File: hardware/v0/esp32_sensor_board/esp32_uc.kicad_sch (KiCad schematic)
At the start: 25 parts, among them J301 USB_B_Micro, J302 Micro_SD_Card_Det, SW301 SW_SPST, U301 ESP32-C3, Y301 40 MHz, Y302 32kHz RTC Crystal

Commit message: Clean up errors
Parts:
- Y301: symbol Device:Crystal_GND24 -> BVH_Crystals:Crystal_GND24
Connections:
- net I2C_SCK: now also U301.10 (MTDI/GPIO5/ADC2_CH0)
- net I2C_SDA: now also U301.9 (MTMS/GPIO4/ADC1_CH4)
- net SD_CS: now also U301.21 (SPICS0/GPIO14)
- net SD_SCK: now also U301.22 (SPICLK/GPIO15)
- no-connect marks 0 -> 2
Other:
- moved on the sheet: C301, C302, C303, C304, C305, C306, C307, C308, C309, C310, C311, C312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

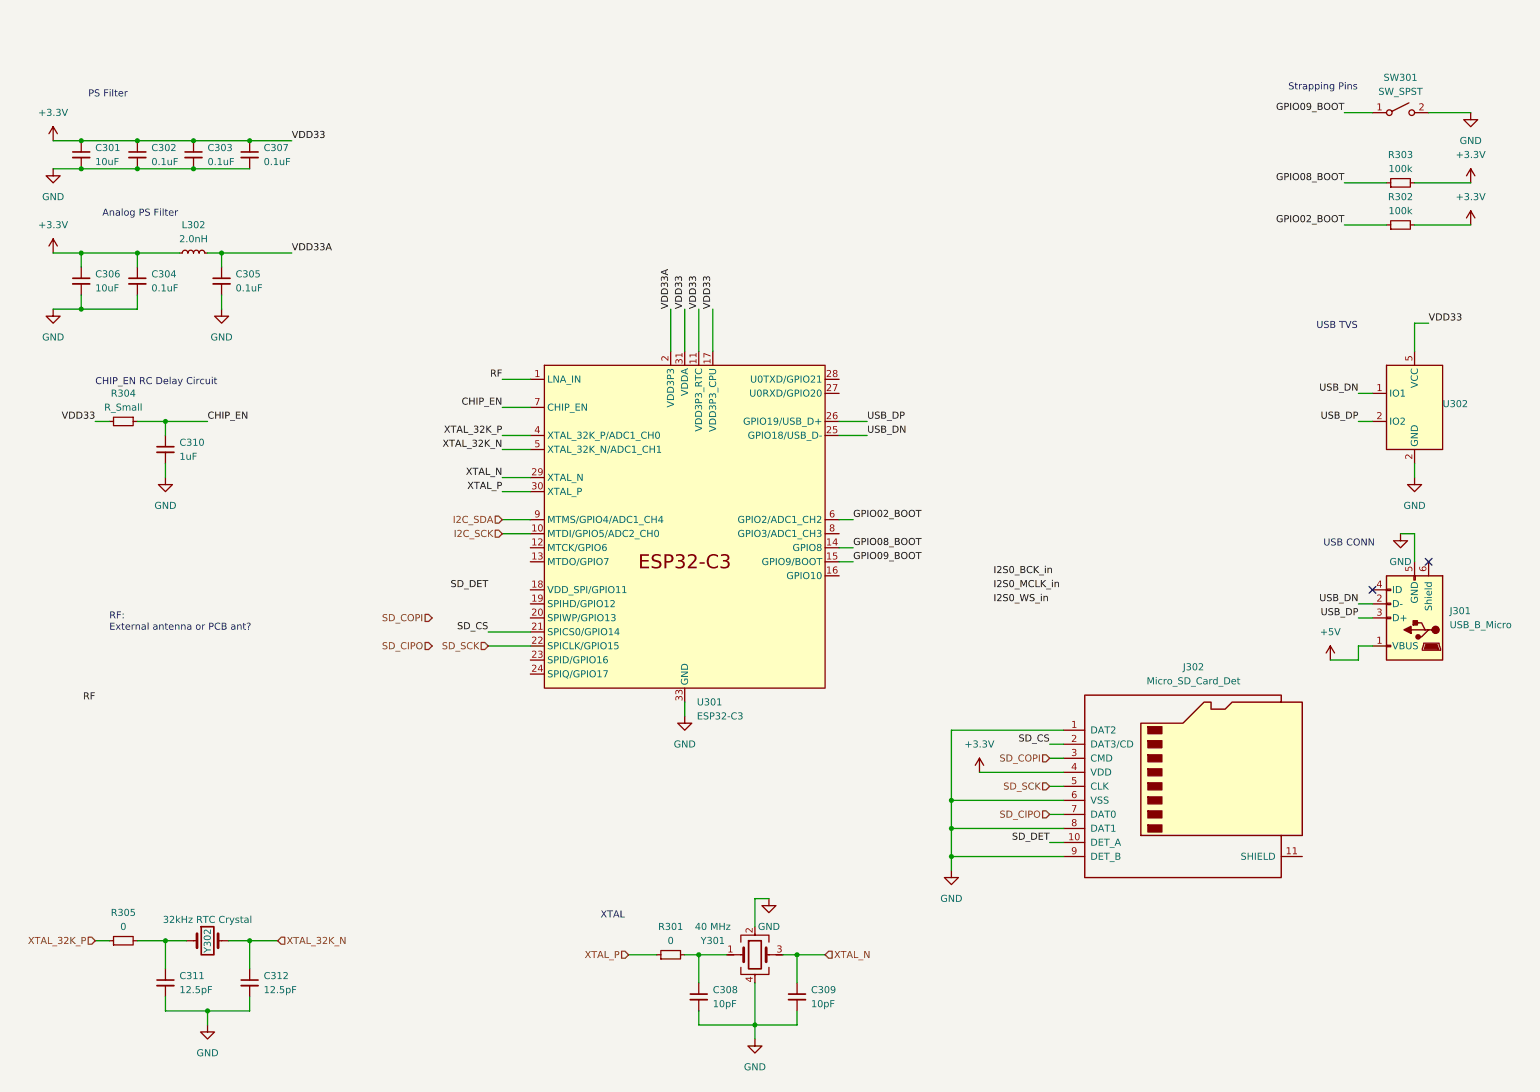
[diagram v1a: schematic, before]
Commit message: PCB ordered, a few initial mistakes fixed
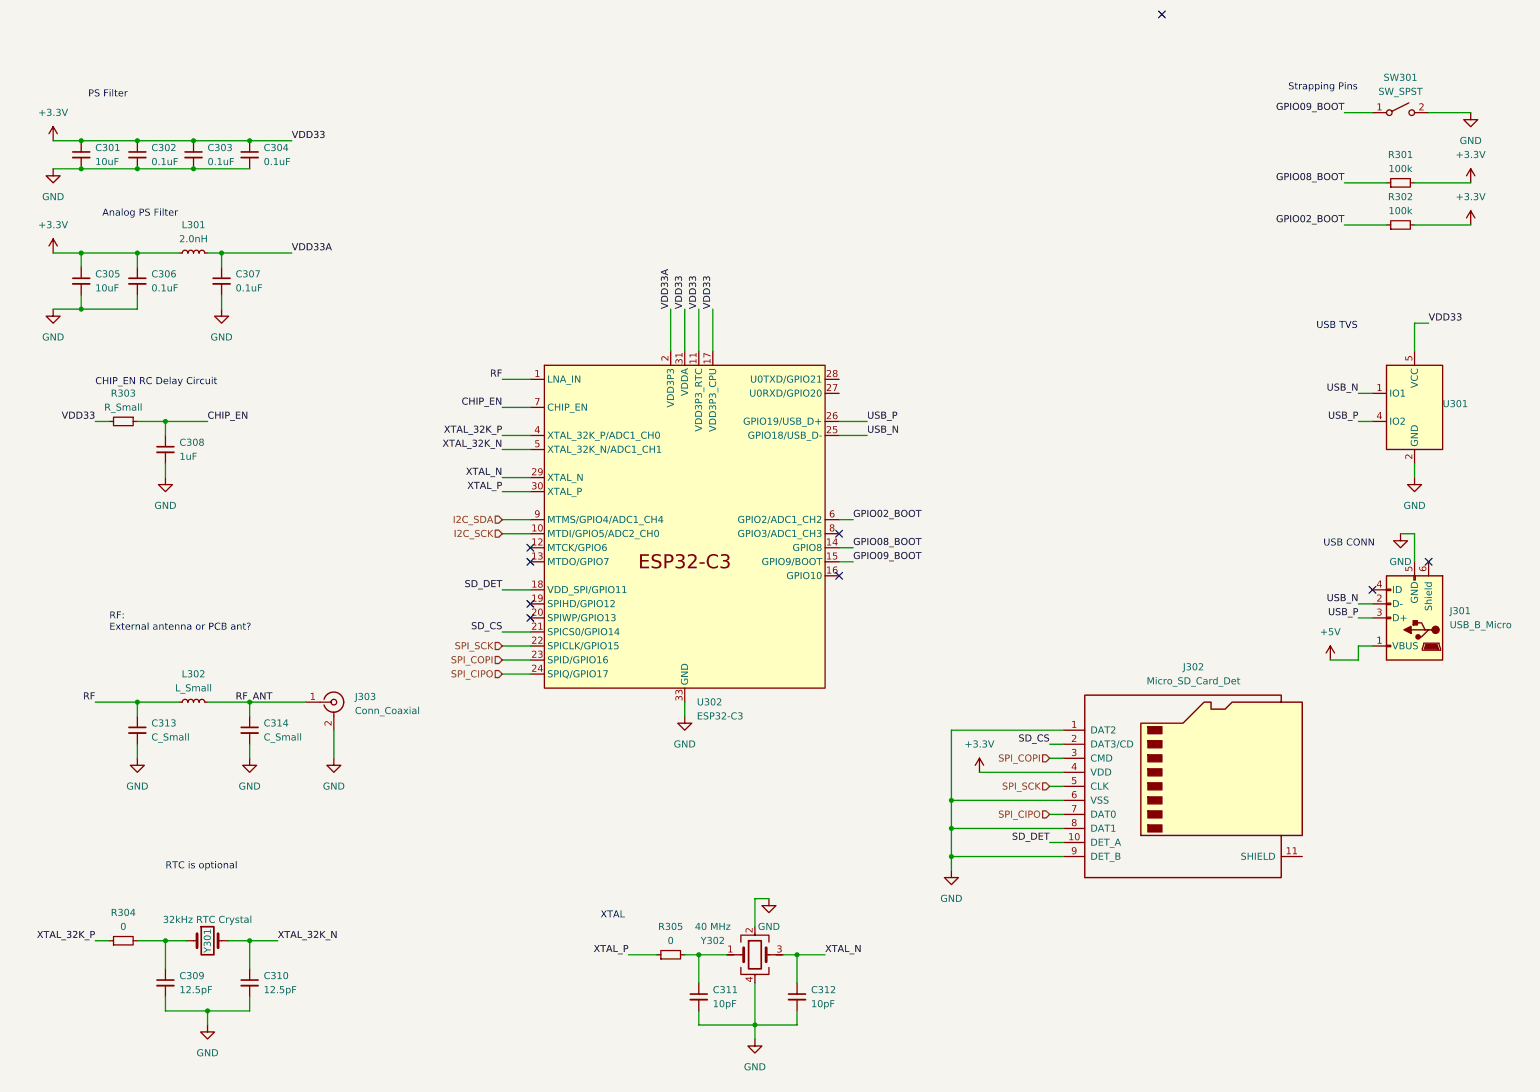
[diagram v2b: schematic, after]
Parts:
- added C313, C314: C_Small, Capacitor_SMD:C_0603_1608Metric, symbol Device:C_Small
- added J303: Conn_Coaxial, Connector_Coaxial:U.FL_Molex_MCRF_73412-0110_Vertical, symbol Connector:Conn_Coaxial
- added L302: L_Small, Inductor_SMD:L_0603_1608Metric, symbol Device:L_Small
- J301: footprint (none) -> Connector_USB:USB_Micro-B_Molex-105017-0001
- J302: footprint (none) -> BVH_Connectors_Misc:MicroSD_Socket_Unbranded
- R303: renamed from R304; footprint (none) -> Resistor_SMD:R_0603_1608Metric
- SW301: footprint (none) -> BVH_Switches:TacButton_SMD_5mm_5mm
- renumbered C307 to C304, C306 to C305, C304 to C306, C305 to C307, C310 to C308, C311 to C309, C312 to C310, C308 to C311, C309 to C312, L302 to L301, R303 to R301, R305 to R304, R301 to R305, U302 to U301, U301 to U302, Y302 to Y301, Y301 to Y302
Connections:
- net SD_CIPO is gone; now on net SPI_CIPO: J302.7 (DAT0)
- net SD_COPI is gone; now on net SPI_COPI: J302.3 (CMD)
- net GND: now also C313.2, C314.2, J303.2 (Ext)
- net RF: now also C313.1, L302.1
- net SD_DET: now also U302.18 (VDD_SPI/GPIO11)
- net SPI_COPI: now reaches U302.23 (SPID/GPIO16)
- net SPI_CIPO: now reaches U302.24 (SPIQ/GPIO17)
- net SD_SCK renamed SPI_SCK
- net USB_DN renamed USB_N
- net USB_DP renamed USB_P
- net USB_P: now also U301.4 (IO2); no longer U301.2 (IO2)
- new net RF_ANT: C314.1, J303.1 (In), L302.2
- no-connect marks 2 -> 9
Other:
- note added: "RTC is optional"

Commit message: WIP
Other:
- note added: "RF: External antenna connector"
- note removed: "RF: External antenna or PCB ant?"
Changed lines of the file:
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@@
     (effects (font (size 1.27 1.27)) (justify left bottom))
   )
-  (text "RF:\nExternal antenna or PCB ant?" (at 30.48 116.84 0)
+  (text "RF:\nExternal antenna connector\n" (at 30.48 116.84 0)
     (effects (font (size 1.27 1.27)) (justify left bottom))
   )

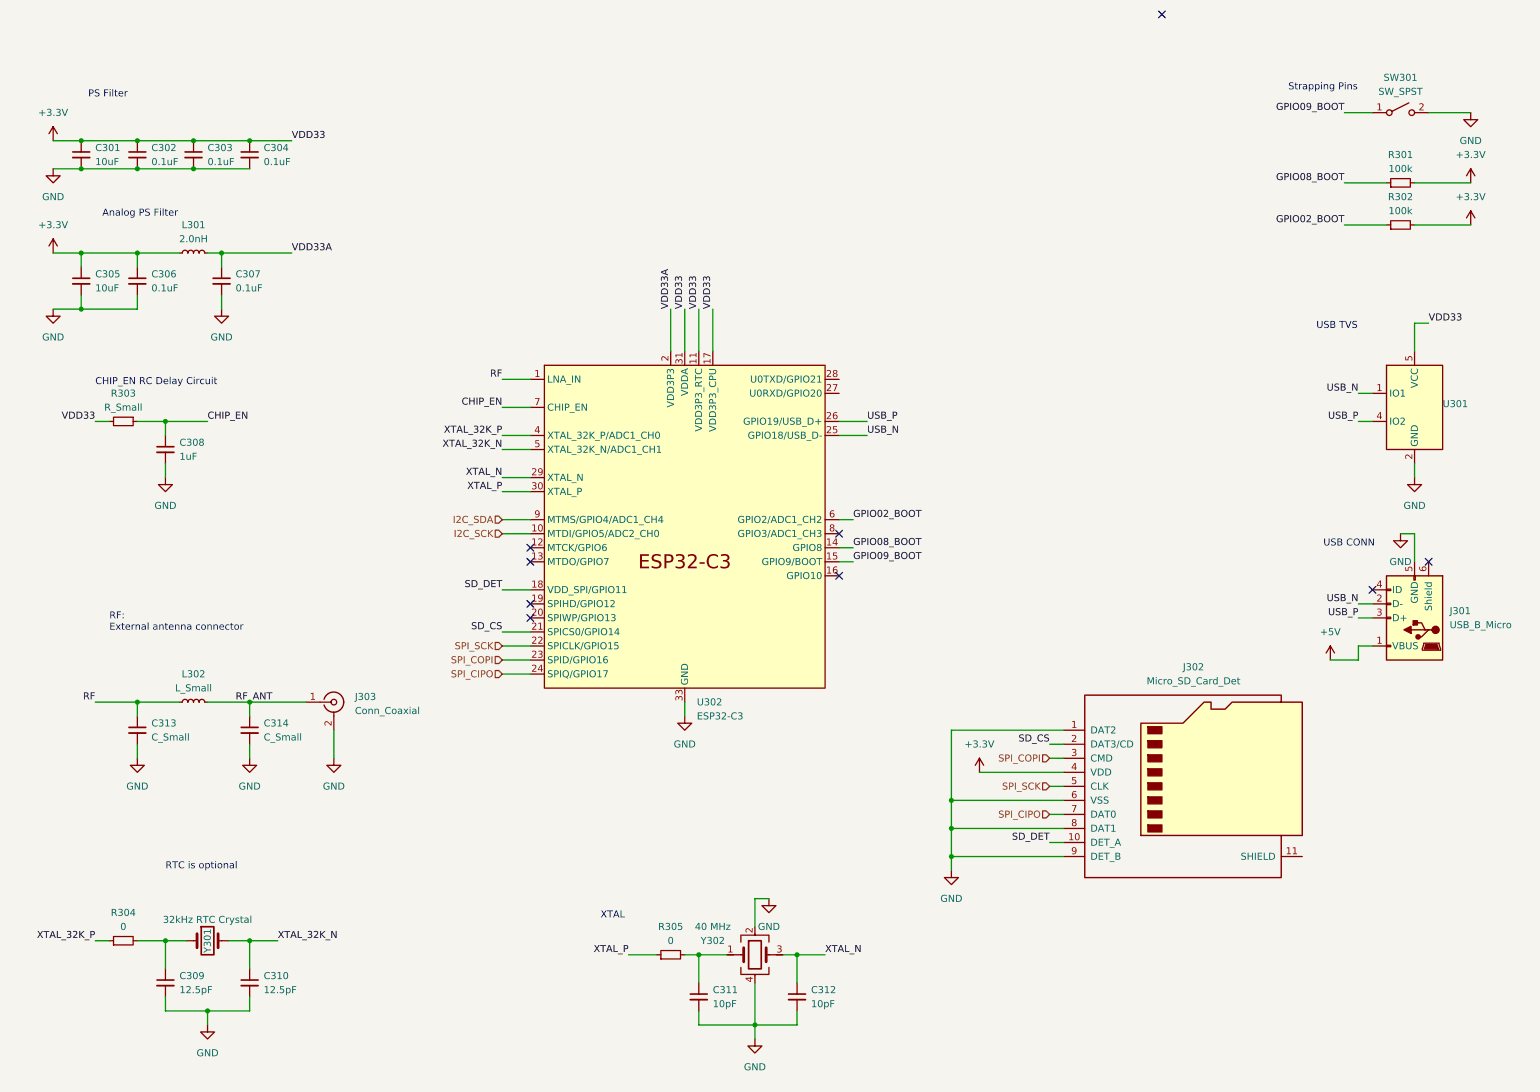
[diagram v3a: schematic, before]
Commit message: Board refactor WIP.  Still needs PU resistors
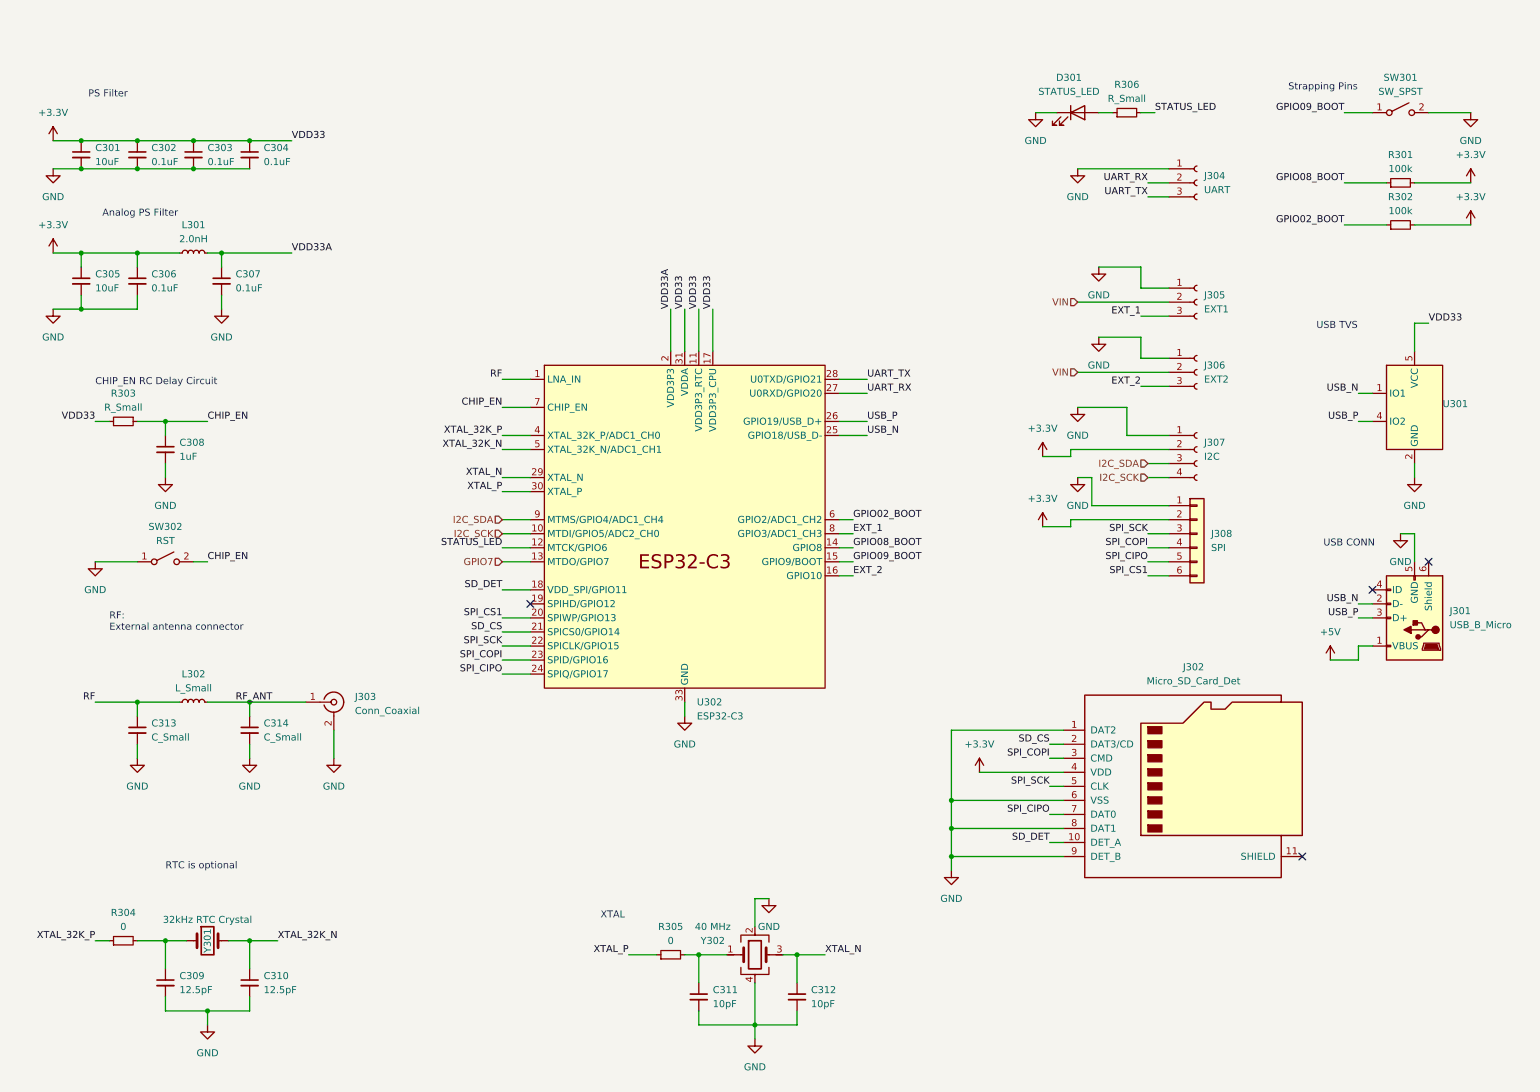
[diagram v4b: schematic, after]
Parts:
- added D301: STATUS_LED, LED_SMD:LED_0805_2012Metric, symbol Device:LED
- added J304: UART, Connector_PinHeader_2.54mm:PinHeader_1x03_P2.54mm_Vertical, symbol Connector:Conn_01x03_Socket
- added J305: EXT1, Connector_PinHeader_2.54mm:PinHeader_1x03_P2.54mm_Vertical, symbol Connector:Conn_01x03_Socket
- added J306: EXT2, Connector_PinHeader_2.54mm:PinHeader_1x03_P2.54mm_Vertical, symbol Connector:Conn_01x03_Socket
- added J307: I2C, Connector_PinHeader_2.54mm:PinHeader_1x04_P2.54mm_Vertical, symbol Connector:Conn_01x04_Socket
- added J308: SPI, Connector_PinHeader_2.54mm:PinHeader_1x06_P2.54mm_Vertical, symbol Connector_Generic:Conn_01x06
- added R306: R_Small, Resistor_SMD:R_0603_1608Metric, symbol Device:R_Small
- added SW302: RST, BVH_Switches:Tac_SMD_6.4mm_Side_SPST_NO, symbol Switch:SW_SPST
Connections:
- net +3.3V: now also J307.2 (Pin_2), J308.2 (Pin_2)
- net CHIP_EN: now also SW302.2 (B)
- net GND: now also D301.1 (K), J304.1 (Pin_1), J305.1 (Pin_1), J306.1 (Pin_1), J307.1 (Pin_1), J308.1 (Pin_1), SW302.1 (A)
- net I2C_SCK: now also J307.4 (Pin_4)
- net I2C_SDA: now also J307.3 (Pin_3)
- net SPI_CIPO: now also J308.5 (Pin_5)
- net SPI_COPI: now also J308.4 (Pin_4)
- net SPI_SCK: now also J308.3 (Pin_3)
- net STATUS_LED: now reaches U302.12 (MTCK/GPIO6)
- net STATUS_LED: now also R306.2
- net GPIO7: now reaches U302.13 (MTDO/GPIO7)
- net EXT_2: now reaches U302.16 (GPIO10)
- net EXT_2: now also J306.3 (Pin_3)
- net SPI_CS1: now reaches U302.20 (SPIWP/GPIO13)
- net SPI_CS1: now also J308.6 (Pin_6)
- net UART_RX: now reaches U302.27 (U0RXD/GPIO20)
- net UART_RX: now also J304.2 (Pin_2)
- net UART_TX: now reaches U302.28 (U0TXD/GPIO21)
- net UART_TX: now also J304.3 (Pin_3)
- net EXT_1: now reaches U302.8 (GPIO3/ADC1_CH3)
- net EXT_1: now also J305.3 (Pin_3)
- new net: D301.2 (A), R306.1
- new net VIN: J305.2 (Pin_2), J306.2 (Pin_2)
- no-connect marks 9 -> 4

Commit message: TVS and PU work
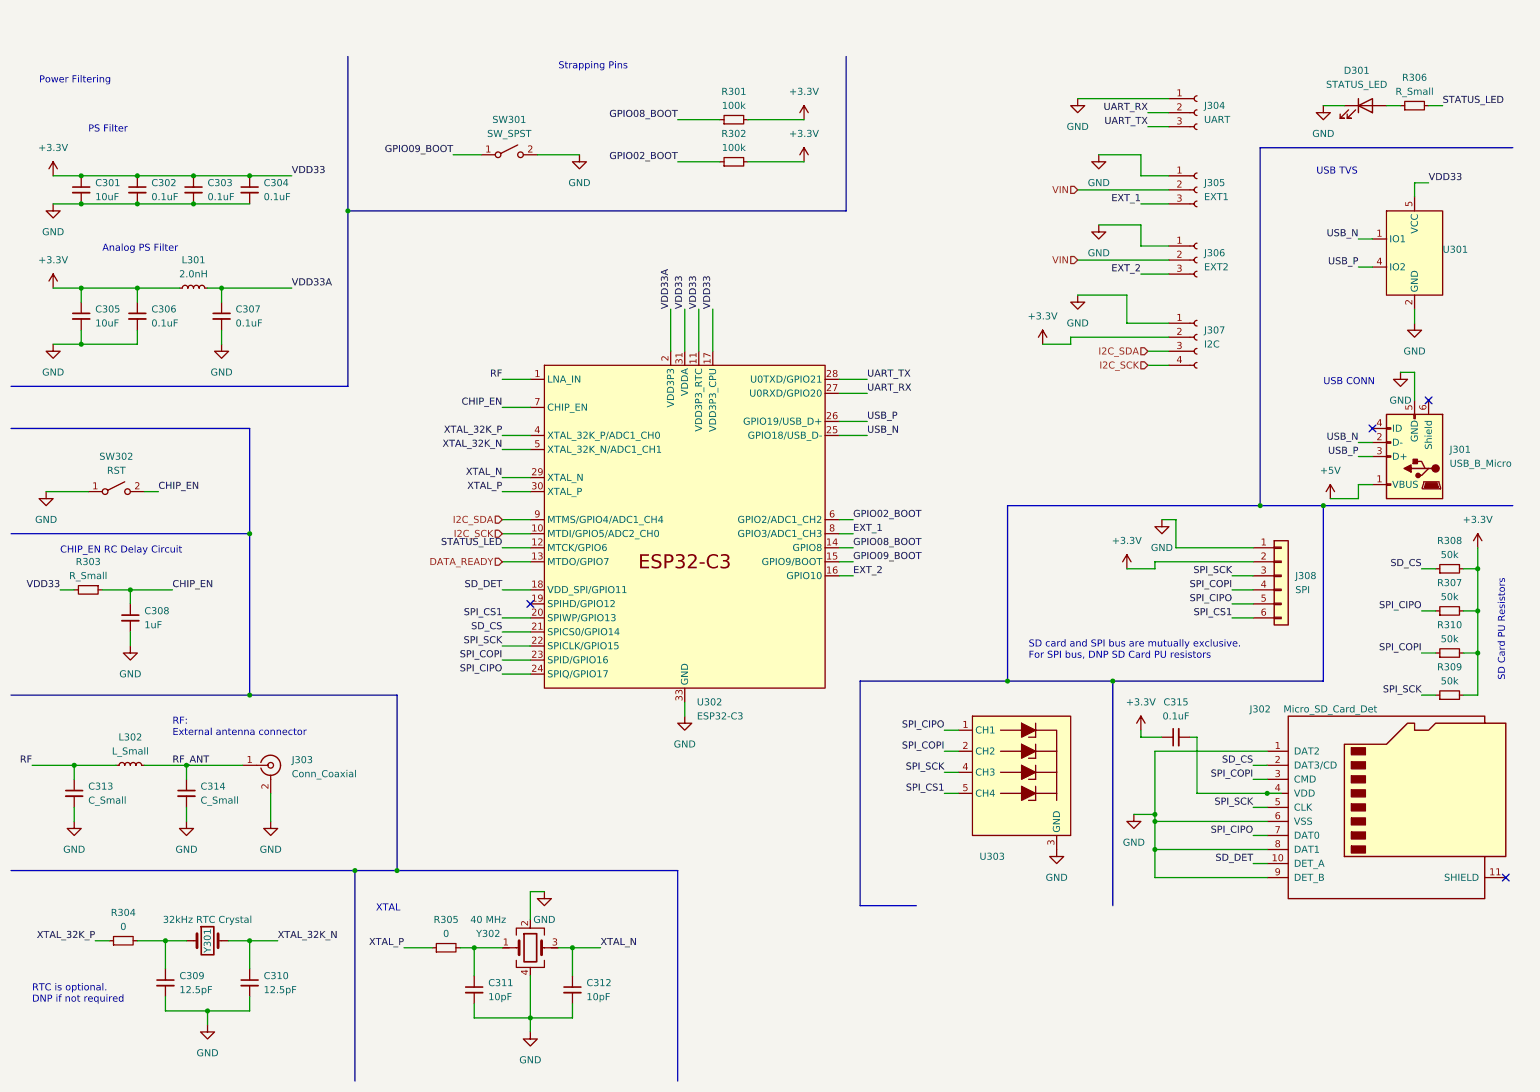
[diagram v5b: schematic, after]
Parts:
- added C315: 0.1uF, Capacitor_SMD:C_0603_1608Metric, symbol Device:C_Small
- added R307, R308, R309, R310: 50k, Resistor_SMD:R_0603_1608Metric, symbol Device:R_Small
- added U303: ~, BVH_Components_Misc:Diode_10Pin_DFN2510A-10_10-XFDFN_SOT1176-1, symbol BVH_Protection:PUSB3AB4
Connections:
- net +3.3V: now also C315.1, R307.2, R308.2, R309.2, R310.2; no longer J302.4 (VDD)
- net GND: now also U303.3 (GND), U303.8 (GND)
- net SD_CS: now also R308.1
- net SPI_CIPO: now also R307.1, U303.1 (CH1)
- net SPI_COPI: now also R310.1, U303.2 (CH2)
- net SPI_CS1: now also U303.5 (CH4)
- net SPI_SCK: now also R309.1, U303.4 (CH3)
- net GPIO7 renamed DATA_READY
- new net: C315.2, J302.4 (VDD)
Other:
- note added: "Power Filtering"
- note added: "RTC is optional. DNP if not required"
- note added: "SD Card PU Resistors"
- note added: "SD card and SPI bus are mutually exclusive. For SPI bus, DNP SD Card PU resistors"
- note removed: "RTC is optional"
- moved on the sheet: C301, C302, C303, C304, C305, C306, C307, C308, C311, C312, C313, C314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
